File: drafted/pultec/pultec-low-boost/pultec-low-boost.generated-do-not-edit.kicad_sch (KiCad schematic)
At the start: 19 parts, among them J1 Conn_01x05, J2 Conn_01x05, SW1 6-way selector

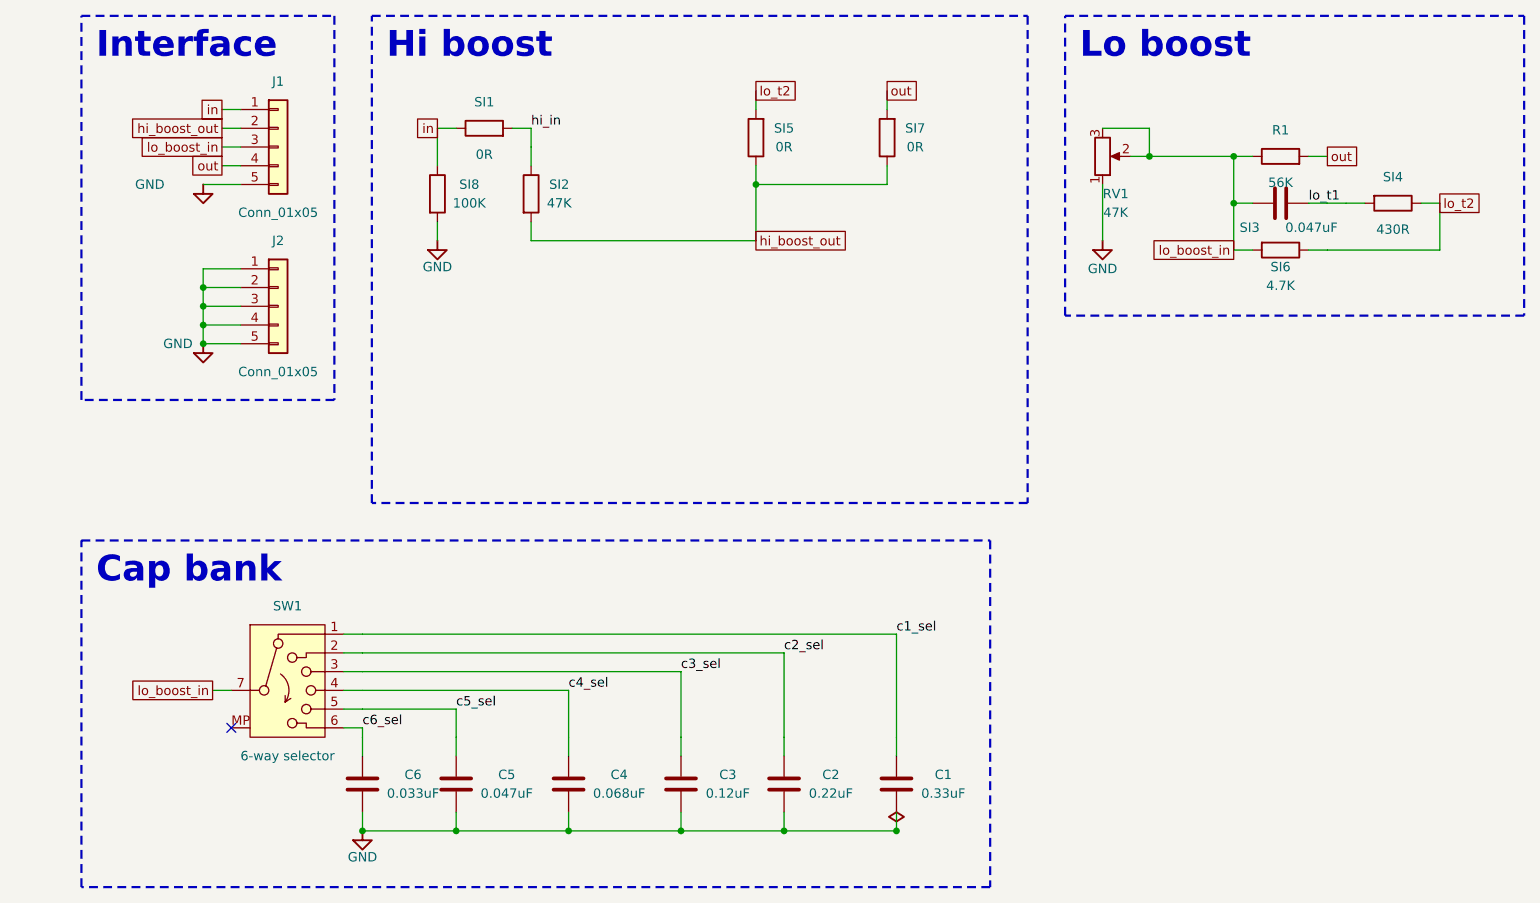
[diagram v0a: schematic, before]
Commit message: Centre all five Pultec pages, promote the two that were not in drafted/
At the owner's directive, 2026-10-30: "It's goofy but serviceable. You need to
center the content in the horizontal (long) axis", and "yes" to centring the
other four.

Promoted the approved centred pultec-hi-cut Letter sheet and the re-drawn
pultec-mid Letter sheet into drafted/pultec/, both byte-for-byte against their
stated source hashes. All five sheets now carry (paper "USLetter"); mid's
promoted sheet already did, so no paper edit was needed anywhere.

Offsets, against an inner frame re-derived two ways as x 12.0 .. 267.4:
hi-boost +9.5250 east, low-boost -8.8900 west, low-cut -8.2550 west,
hi-cut 0, mid 0. hi-cut computing zero is the check the task asked for - the
approved page is already centred, and the run asserts its bytes are unchanged
rather than assuming it. mid computes zero too, and is exactly centred rather
than nearly: its content midpoint is 139.700 mm and so is the frame's.

Each translation is proved rigid geometrically and electrically, every check
with a positive control that reported a difference. Four defects were found in
the centring script while committing it out of a scratchpad, the sharpest being
that its zero-offset byte-identity guard tested dx == 0 and so was DEAD on the
two sheets it exists to protect, an already-centred sheet giving -7e-15.

pultec-mid's previous committed render was the one of the five exported without
--black-and-white, carrying 18 colours; proved by reproducing its old digest
from a no-flag export. All five renders are now on one recipe.

hi-cut's RECORD.md records his approval, quoting him. The other four say
awaiting re-approval. docs/schematic/verdicts.md is deliberately not edited: it
already records what he said and what it does not cover.

All five build guides regenerated; the page-one paper notice has cleared on
every one, with a control proving the detector can see it. Every page of every
guide.pdf is now US Letter.

typecheck clea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
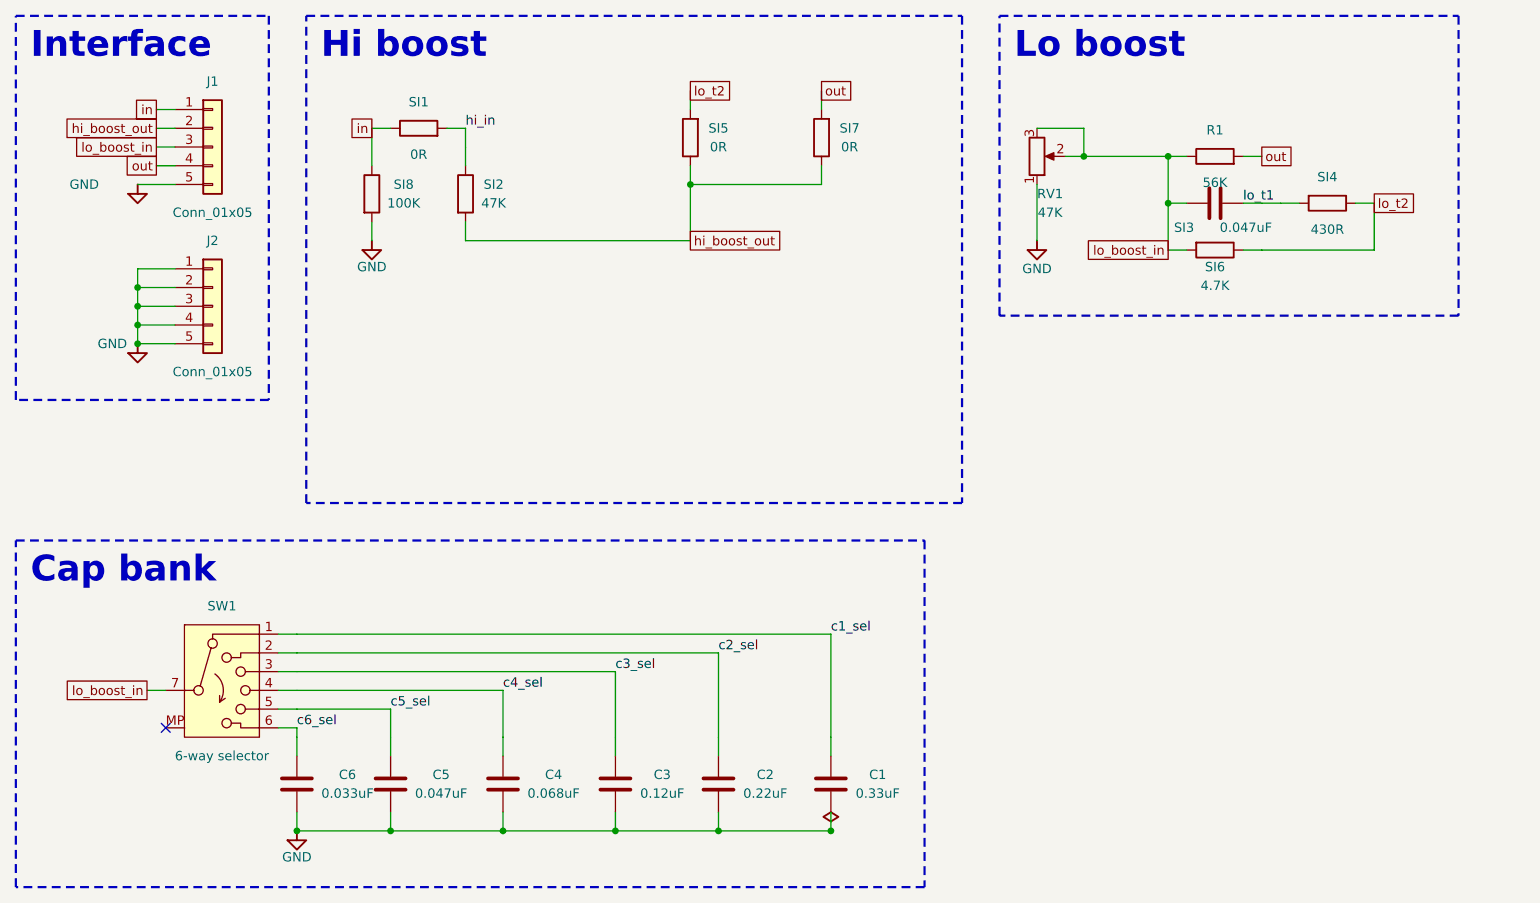
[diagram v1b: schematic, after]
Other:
- moved on the sheet: C1, C2, C3, C4, C5, C6, J1, J2, R1, RV1, SI1, SI2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
